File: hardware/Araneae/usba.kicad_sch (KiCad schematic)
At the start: 15 parts, among them J4 USB_A_Stacked, J5 USB_A, U10 TPS2041B, U8 TPS2041B, U9 TPS2041B

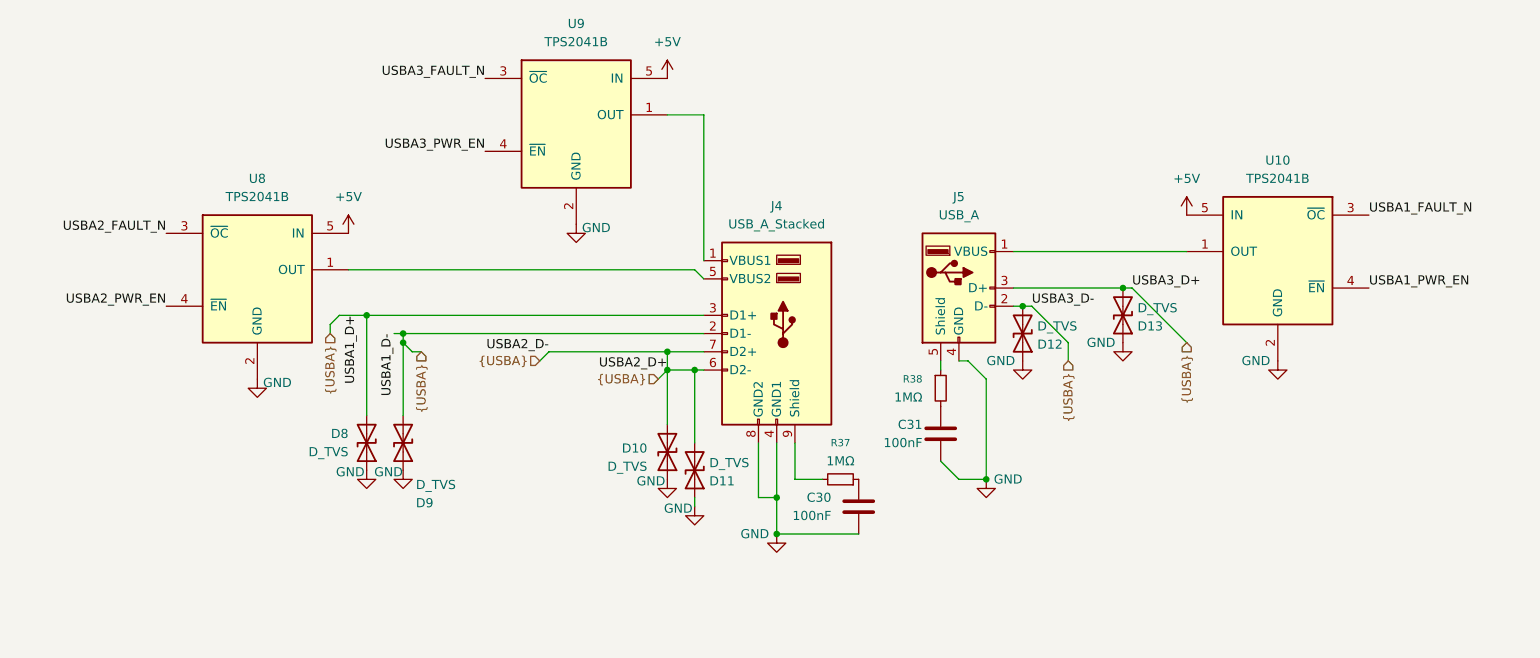
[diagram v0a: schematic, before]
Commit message: Add CI workflow for PCB checks and artifact generation
- Created a GitHub Actions workflow (`ci.yml`) to automate hardware checks including ERC, DRC, and plot generation for KiCad projects.
- Added a new footprint for the SON50P200X200X80-9N component in `SON50P200X200X80-9N.kicad_mod`.
- Introduced a new symbol for the TPS22965DSGR component in `TPS22965DSGR.kicad_sym`.
- Added a configuration file `kibot.yaml` for generating fabrication files and other outputs.
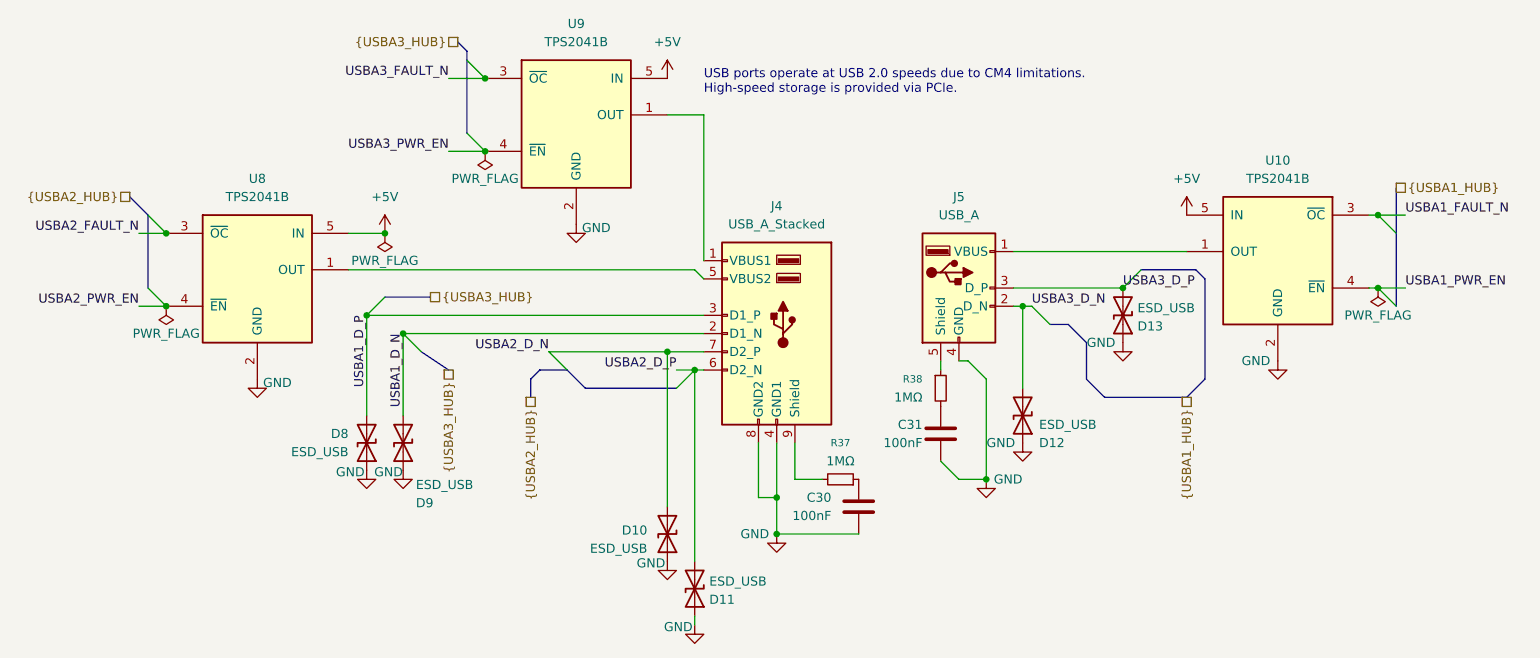
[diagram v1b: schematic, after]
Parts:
- C30, C31: footprint (none) -> Capacitor_SMD:C_0603_1608Metric
- D10, D11, D12, D13, D8, D9: value D_TVS -> ESD_USB; footprint (none) -> Diode_SMD:D_SOD-323
- J5: footprint (none) -> Connector_USB:USB_A_Wuerth_614004134726_Horizontal
- R37, R38: footprint (none) -> Resistor_SMD:R_0603_1608Metric
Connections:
- removed net {USBA}: D10.2 (A2), D11.2 (A2), D12.2 (A2), D13.2 (A2), D8.2 (A2), D9.2 (A2), J4.2 (D1-), J4.3 (D1+), J4.6 (D2-), J4.7 (D2+), J5.2 (D-), J5.3 (D+)
- new net USBA1_D_N: D9.2 (A2), J4.2 (D1_N)
- new net USBA1_D_P: D8.2 (A2), J4.3 (D1_P)
- new net USBA2_D_N: D10.2 (A2), J4.7 (D2_P)
- new net USBA2_D_P: D11.2 (A2), J4.6 (D2_N)
- new net USBA3_D_N: D12.2 (A2), J5.2 (D_N)
- new net USBA3_D_P: D13.2 (A2), J5.3 (D_P)
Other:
- note added: "USB ports operate at USB 2.0 speeds due to CM4 limitations. High-speed storage is provided via PCIe."
- company: (none) -> Matheus Henrique(Aka: TheusHen)
- title: (none) -> Araneae
- moved on the sheet: D10, D11, D12
